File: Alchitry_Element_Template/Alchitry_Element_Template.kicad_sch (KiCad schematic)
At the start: 1 part

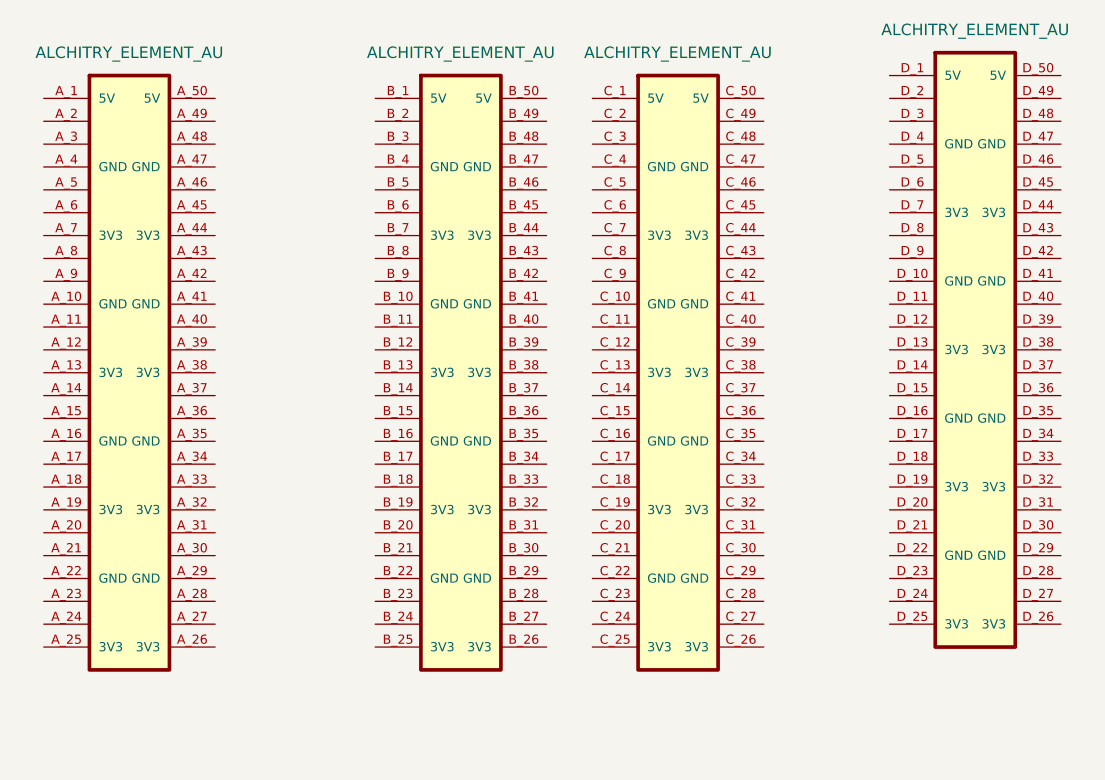
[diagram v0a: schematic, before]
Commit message: rename library and change folder structure
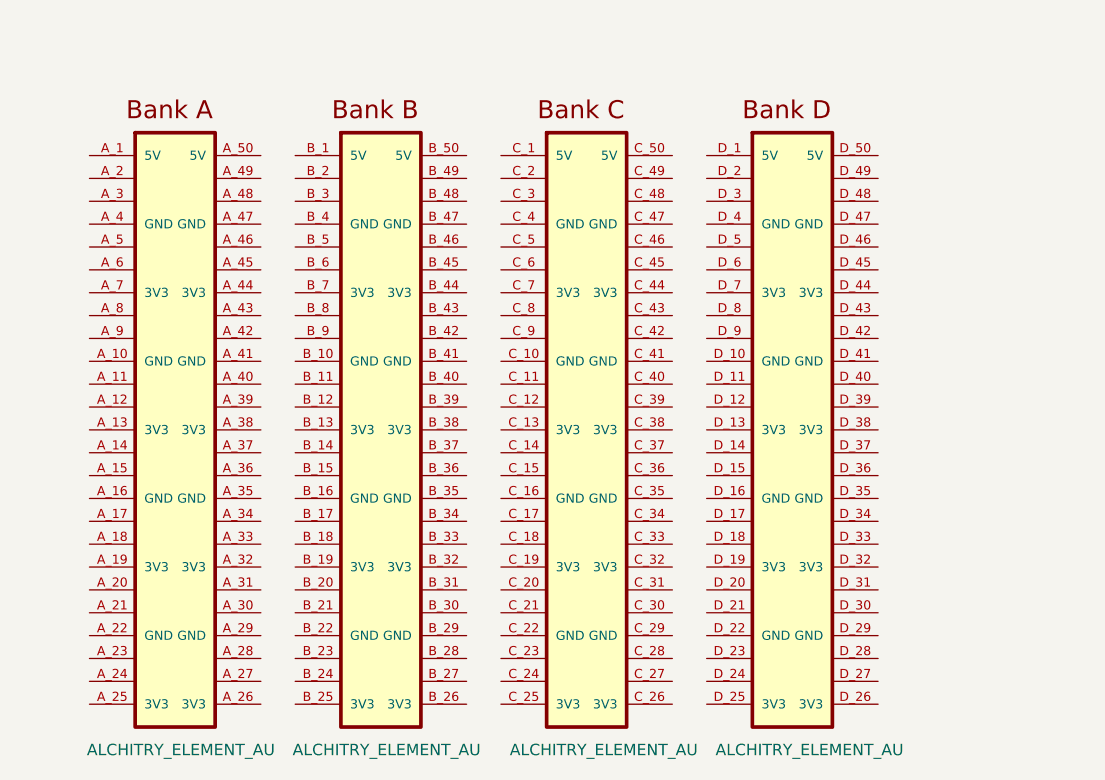
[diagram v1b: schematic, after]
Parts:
- B1: symbol ALCHITRY_ELEMENT:ALCHITRY_ELEMENT_AU -> Alchitry_Element:Alchitry_Element_AU
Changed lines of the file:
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@@
 (kicad_sch (version 20211123) (generator eeschema)
   (paper "A4")
-  (symbol (lib_id "ALCHITRY_ELEMENT:ALCHITRY_ELEMENT_AU") (at 90.17 50.8 0) (unit 3)
-    (in_bom yes) (on_board yes) (fields_autoplaced)
-    (property "Reference" "B1" (id 0) (at 86.36 19.558 0)
+  (symbol (lib_name "Alchitry_Element_AU_3") (lib_id "Alchitry_Element:Alchitry_Element_AU") (at 80.01 57.15 0) (unit 3)
+    (in_bom yes) (on_board yes)
+    (property "Reference" "B1" (id 0) (at 76.2 25.908 0)
       (effects (font (size 1.27 1.27)) (justify left bottom) hide)
     )
-    (property "Value" "ALCHITRY_ELEMENT_AU" (id 1) (at 90.805 17.78 0))
-    (property "Footprint" "ALCHITRY_ELEMENT:ELEMENT" (id 2) (at 90.17 50.8 0)
-      (effects (font (size 1.27 1.27)) hide)
-    )
-    (property "Datasheet" "" (id 3) (at 90.17 50.8 0)
+    (property "Value" "ALCHITRY_ELEMENT_AU" (id 1) (at 82.55 95.25 0))
+    (property "Footprint" "ALCHITRY_ELEMENT:ELEMENT" (id 2) (at 80.01 57.15 0)
+      (effects (font (size 1.27 1.27)) hide)
+    )
+    (property "Datasheet" "" (id 3) (at 80.01 57.15 0)
       (effects (font (size 1.27 1.27)) hide)
     )
@@
     (pin "D_9")
   )
-  (symbol (lib_id "ALCHITRY_ELEMENT:ALCHITRY_ELEMENT_AU") (at 66.04 50.8 0) (unit 2)
-    (in_bom yes) (on_board yes) (fields_autoplaced)
-    (property "Reference" "B1" (id 0) (at 62.23 19.558 0)
+  (symbol (lib_name "Alchitry_Element_AU_1") (lib_id "Alchitry_Element:Alchitry_Element_AU") (at 57.15 57.15 0) (unit 2)
+    (in_bom yes) (on_board yes)
+    (property "Reference" "B1" (id 0) (at 53.34 25.908 0)
       (effects (font (size 1.27 1.27)) (justify left bottom) hide)
     )
-    (property "Value" "ALCHITRY_ELEMENT_AU" (id 1) (at 66.675 17.78 0))
-    (property "Footprint" "ALCHITRY_ELEMENT:ELEMENT" (id 2) (at 66.04 50.8 0)
-      (effects (font (size 1.27 1.27)) hide)
-    )
-    (property "Datasheet" "" (id 3) (at 66.04 50.8 0)
+    (property "Value" "ALCHITRY_ELEMENT_AU" (id 1) (at 58.42 95.25 0))
+    (property "Footprint" "ALCHITRY_ELEMENT:ELEMENT" (id 2) (at 57.15 57.15 0)
+      (effects (font (size 1.27 1.27)) hide)
+    )
+    (property "Datasheet" "" (id 3) (at 57.15 57.15 0)
       (effects (font (size 1.27 1.27)) hide)
     )
@@
     (pin "D_9")
   )
-  (symbol (lib_id "ALCHITRY_ELEMENT:ALCHITRY_ELEMENT_AU") (at 123.19 48.26 0) (unit 4)
-    (in_bom yes) (on_board yes) (fields_autoplaced)
-    (property "Reference" "B1" (id 0) (at 119.38 17.018 0)
+  (symbol (lib_name "Alchitry_Element_AU_2") (lib_id "Alchitry_Element:Alchitry_Element_AU") (at 102.87 57.15 0) (unit 4)
+    (in_bom yes) (on_board yes)
+    (property "Reference" "B1" (id 0) (at 99.06 25.908 0)
       (effects (font (size 1.27 1.27)) (justify left bottom) hide)
     )
-    (property "Value" "ALCHITRY_ELEMENT_AU" (id 1) (at 123.825 15.24 0))
-    (property "Footprint" "ALCHITRY_ELEMENT:ELEMENT" (id 2) (at 123.19 48.26 0)
-      (effects (font (size 1.27 1.27)) hide)
-    )
-    (property "Datasheet" "" (id 3) (at 123.19 48.26 0)
+    (property "Value" "ALCHITRY_ELEMENT_AU" (id 1) (at 105.41 95.25 0))
+    (property "Footprint" "ALCHITRY_ELEMENT:ELEMENT" (id 2) (at 102.87 57.15 0)
+      (effects (font (size 1.27 1.27)) hide)
+    )
+    (property "Datasheet" "" (id 3) (at 102.87 57.15 0)
       (effects (font (size 1.27 1.27)) hide)
     )
@@
     (pin "D_9")
   )
-  (symbol (lib_id "ALCHITRY_ELEMENT:ALCHITRY_ELEMENT_AU") (at 29.21 50.8 0) (unit 1)
-    (in_bom yes) (on_board yes) (fields_autoplaced)
-    (property "Reference" "B1" (id 0) (at 25.4 19.558 0)
+  (symbol (lib_id "Alchitry_Element:Alchitry_Element_AU") (at 34.29 57.15 0) (unit 1)
+    (in_bom yes) (on_board yes)
+    (property "Reference" "B1" (id 0) (at 30.48 25.908 0)
       (effects (font (size 1.27 1.27)) (justify left bottom) hide)
     )
-    (property "Value" "ALCHITRY_ELEMENT_AU" (id 1) (at 29.845 17.78 0))
-    (property "Footprint" "ALCHITRY_ELEMENT:ELEMENT" (id 2) (at 29.21 50.8 0)
-      (effects (font (size 1.27 1.27)) hide)
-    )
-    (property "Datasheet" "" (id 3) (at 29.21 50.8 0)
-      (effects (font (size 1.27 1.27)) hide)
-    )
+    (property "Value" "ALCHITRY_ELEMENT_AU" (id 1) (at 35.56 95.25 0))
+    (property "Footprint" "ALCHITRY_ELEMENT:ELEMENT" (id 2) (at 34.29 57.15 0)
+      (effects (font (size 1.27 1.27)) hide)
+    )
+    (property "Datasheet" "" (id 3) (at 34.29 57.15 0)
+      (effects (font (size 1.27 1.27)) hide)
+    )

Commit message: add pin names to au symbol
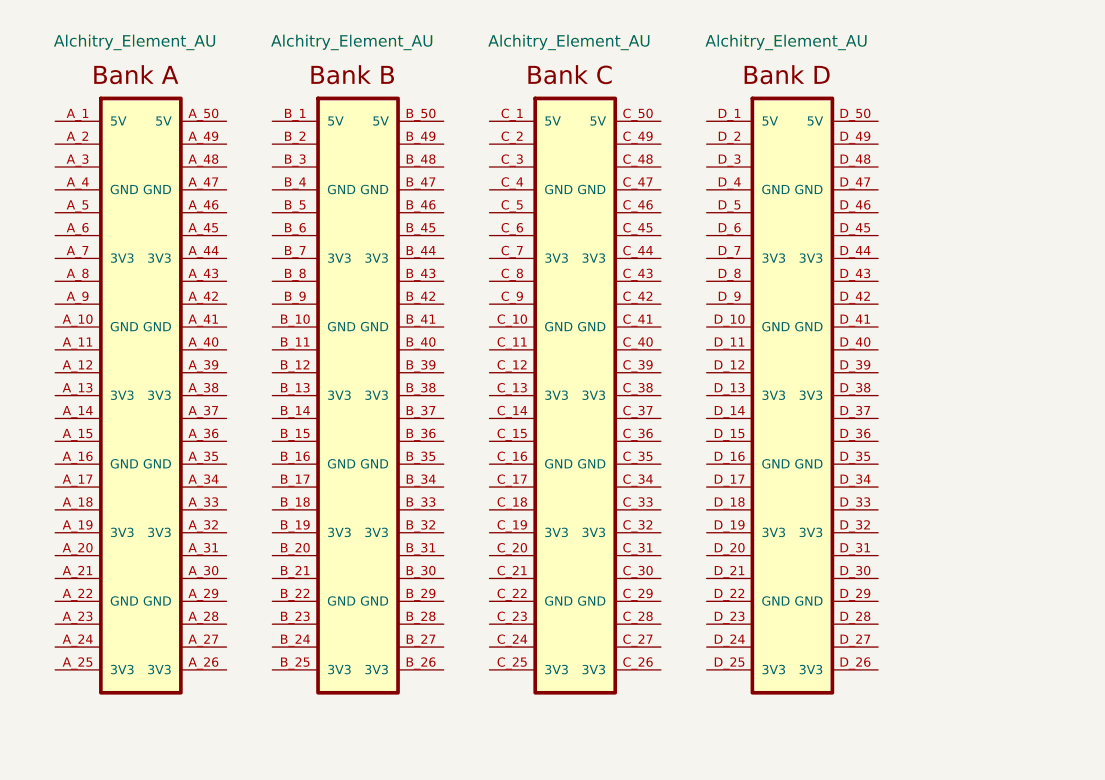
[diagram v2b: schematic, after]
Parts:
- B1: value ALCHITRY_ELEMENT_AU -> Alchitry_Element_AU; footprint ALCHITRY_ELEMENT:ELEMENT -> Alchitry_Element:Element
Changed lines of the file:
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@@
 (kicad_sch (version 20211123) (generator eeschema)
   (paper "A4")
-  (symbol (lib_name "Alchitry_Element_AU_3") (lib_id "Alchitry_Element:Alchitry_Element_AU") (at 80.01 57.15 0) (unit 3)
-    (in_bom yes) (on_board yes)
-    (property "Reference" "B1" (id 0) (at 76.2 25.908 0)
+  (symbol (lib_id "Alchitry_Element:Alchitry_Element_AU") (at 102.87 53.34 0) (unit 4)
+    (in_bom yes) (on_board yes) (fields_autoplaced)
+    (property "Reference" "B1" (id 0) (at 99.06 22.098 0)
       (effects (font (size 1.27 1.27)) (justify left bottom) hide)
     )
-    (property "Value" "ALCHITRY_ELEMENT_AU" (id 1) (at 82.55 95.25 0))
-    (property "Footprint" "ALCHITRY_ELEMENT:ELEMENT" (id 2) (at 80.01 57.15 0)
+    (property "Value" "Alchitry_Element_AU" (id 1) (at 102.87 16.51 0))
+    (property "Footprint" "Alchitry_Element:Element" (id 2) (at 102.87 53.34 0)
       (effects (font (size 1.27 1.27)) hide)
     )
-    (property "Datasheet" "" (id 3) (at 80.01 57.15 0)
+    (property "Datasheet" "" (id 3) (at 102.87 53.34 0)
       (effects (font (size 1.27 1.27)) hide)
     )
@@
     (pin "D_9")
   )
-  (symbol (lib_name "Alchitry_Element_AU_1") (lib_id "Alchitry_Element:Alchitry_Element_AU") (at 57.15 57.15 0) (unit 2)
-    (in_bom yes) (on_board yes)
-    (property "Reference" "B1" (id 0) (at 53.34 25.908 0)
+  (symbol (lib_id "Alchitry_Element:Alchitry_Element_AU") (at 78.74 53.34 0) (unit 3)
+    (in_bom yes) (on_board yes) (fields_autoplaced)
+    (property "Reference" "B1" (id 0) (at 74.93 22.098 0)
       (effects (font (size 1.27 1.27)) (justify left bottom) hide)
     )
-    (property "Value" "ALCHITRY_ELEMENT_AU" (id 1) (at 58.42 95.25 0))
-    (property "Footprint" "ALCHITRY_ELEMENT:ELEMENT" (id 2) (at 57.15 57.15 0)
+    (property "Value" "Alchitry_Element_AU" (id 1) (at 78.74 16.51 0))
+    (property "Footprint" "Alchitry_Element:Element" (id 2) (at 78.74 53.34 0)
       (effects (font (size 1.27 1.27)) hide)
     )
-    (property "Datasheet" "" (id 3) (at 57.15 57.15 0)
+    (property "Datasheet" "" (id 3) (at 78.74 53.34 0)
       (effects (font (size 1.27 1.27)) hide)
     )
@@
     (pin "D_9")
   )
-  (symbol (lib_name "Alchitry_Element_AU_2") (lib_id "Alchitry_Element:Alchitry_Element_AU") (at 102.87 57.15 0) (unit 4)
-    (in_bom yes) (on_board yes)
-    (property "Reference" "B1" (id 0) (at 99.06 25.908 0)
+  (symbol (lib_id "Alchitry_Element:Alchitry_Element_AU") (at 30.48 53.34 0) (unit 1)
+    (in_bom yes) (on_board yes) (fields_autoplaced)
+    (property "Reference" "B1" (id 0) (at 26.67 22.098 0)
       (effects (font (size 1.27 1.27)) (justify left bottom) hide)
     )
-    (property "Value" "ALCHITRY_ELEMENT_AU" (id 1) (at 105.41 95.25 0))
-    (property "Footprint" "ALCHITRY_ELEMENT:ELEMENT" (id 2) (at 102.87 57.15 0)
+    (property "Value" "Alchitry_Element_AU" (id 1) (at 30.48 16.51 0))
+    (property "Footprint" "Alchitry_Element:Element" (id 2) (at 30.48 53.34 0)
       (effects (font (size 1.27 1.27)) hide)
     )
-    (property "Datasheet" "" (id 3) (at 102.87 57.15 0)
+    (property "Datasheet" "" (id 3) (at 30.48 53.34 0)
       (effects (font (size 1.27 1.27)) hide)
     )
@@
     (pin "D_9")
   )
-  (symbol (lib_id "Alchitry_Element:Alchitry_Element_AU") (at 34.29 57.15 0) (unit 1)
-    (in_bom yes) (on_board yes)
-    (property "Reference" "B1" (id 0) (at 30.48 25.908 0)
+  (symbol (lib_id "Alchitry_Element:Alchitry_Element_AU") (at 54.61 53.34 0) (unit 2)
+    (in_bom yes) (on_board yes) (fields_autoplaced)
+    (property "Reference" "B1" (id 0) (at 50.8 22.098 0)
       (effects (font (size 1.27 1.27)) (justify left bottom) hide)
     )
-    (property "Value" "ALCHITRY_ELEMENT_AU" (id 1) (at 35.56 95.25 0))
-    (property "Footprint" "ALCHITRY_ELEMENT:ELEMENT" (id 2) (at 34.29 57.15 0)
+    (property "Value" "Alchitry_Element_AU" (id 1) (at 54.61 16.51 0))
+    (property "Footprint" "Alchitry_Element:Element" (id 2) (at 54.61 53.34 0)
       (effects (font (size 1.27 1.27)) hide)
     )
-    (property "Datasheet" "" (id 3) (at 34.29 57.15 0)
+    (property "Datasheet" "" (id 3) (at 54.61 53.34 0)
       (effects (font (size 1.27 1.27)) hide)
     )
@@
   )
   (symbol_instances
-    (path "/e5f4dadd-6ed8-4220-bf78-b675c64702be"
-      (reference "B1") (unit 1) (value "ALCHITRY_ELEMENT_AU") (footprint "ALCHITRY_ELEMENT:ELEMENT")
-    )
-    (path "/469fb5f9-fe8c-4dc3-a091-c42f51215f76"
-      (reference "B1") (unit 2) (value "ALCHITRY_ELEMENT_AU") (footprint "ALCHITRY_ELEMENT:ELEMENT")
-    )
-    (path "/045706fe-86e7-4d48-bee4-b53470e83ee6"
-      (reference "B1") (unit 3) (value "ALCHITRY_ELEMENT_AU") (footprint "ALCHITRY_ELEMENT:ELEMENT")
-    )
-    (path "/9ce5b3ea-859a-4150-b39d-69fc63ce0919"
-      (reference "B1") (unit 4) (value "ALCHITRY_ELEMENT_AU") (footprint "ALCHITRY_ELEMENT:ELEMENT")
+    (path "/e99c9da9-557b-4ad8-8273-1981e7d093c1"
+      (reference "B1") (unit 1) (value "Alchitry_Element_AU") (footprint "Alchitry_Element:Element")
+    )
+    (path "/fb3014d9-5505-46b0-8a5a-a35e12fa6311"
+      (reference "B1") (unit 2) (value "Alchitry_Element_AU") (footprint "Alchitry_Element:Element")
+    )
+    (path "/64b0a659-cc66-4dab-a5de-a223ad0dd9c7"
+      (reference "B1") (unit 3) (value "Alchitry_Element_AU") (footprint "Alchitry_Element:Element")
+    )
+    (path "/4bdf0009-8cc2-43f7-ad98-25fa71059f32"
+      (reference "B1") (unit 4) (value "Alchitry_Element_AU") (footprint "Alchitry_Element:Element")
     )
   )
